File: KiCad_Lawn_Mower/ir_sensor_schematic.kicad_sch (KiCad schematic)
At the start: 1 part

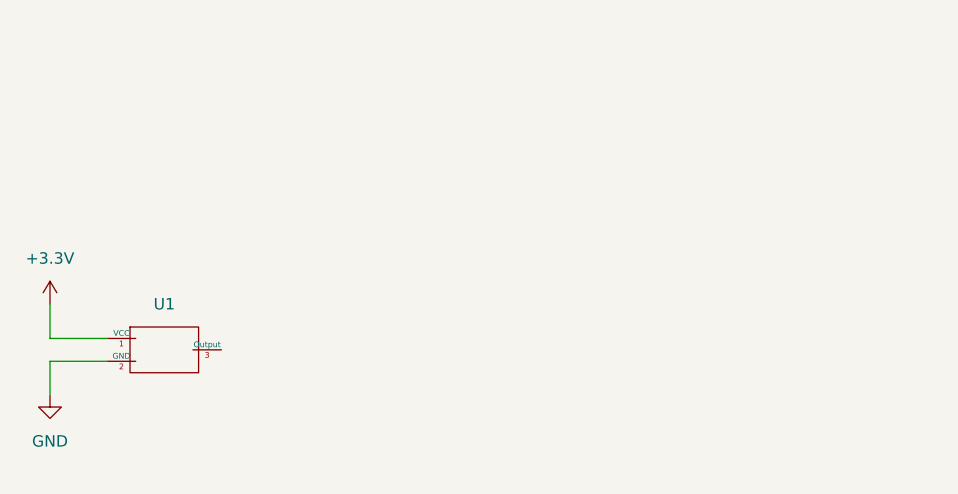
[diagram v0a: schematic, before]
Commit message: Update schematics and system design
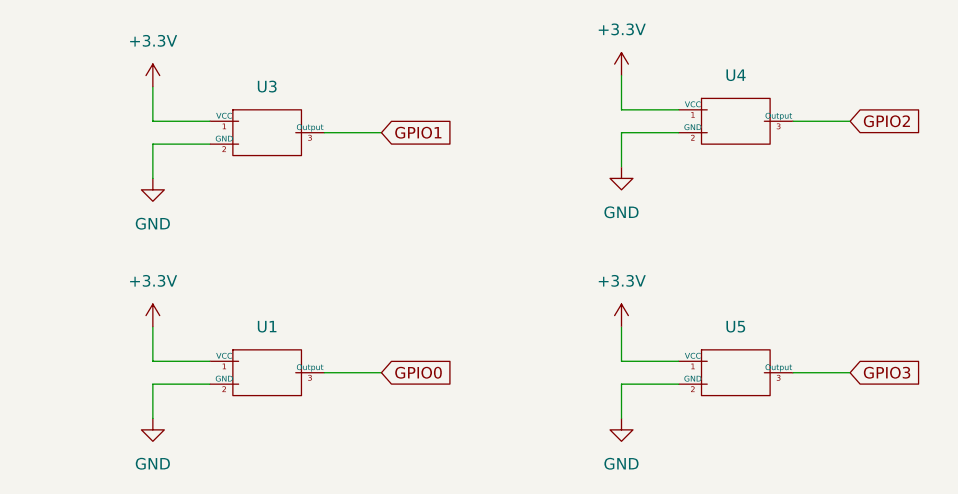
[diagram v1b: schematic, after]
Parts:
- added U3, U4, U5: (no value), Flying fish IR sensor PCB aka FC51, symbol Custom_symbols:IR_Sensor_FC51
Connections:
- net +3.3V: now also U3.1 (VCC), U4.1 (VCC), U5.1 (VCC)
- net GND: now also U3.2 (GND), U4.2 (GND), U5.2 (GND)
- net GPIO0: now reaches U1.3 (Output)
- new net GPIO1: U3.3 (Output)
- new net GPIO2: U4.3 (Output)
- new net GPIO3: U5.3 (Output)
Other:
- moved on the sheet: U1

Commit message: Adding IR sensor init and fixing schematic
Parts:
- added C1, C2, C3, C4: 0.1uF, symbol Device:C_Small
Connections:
- net +3.3V: now also C1.1, C2.1, C3.1, C4.2
- net GND: now also C1.2, C2.2, C3.2, C4.1
- net GPIO0 renamed GPIO4
